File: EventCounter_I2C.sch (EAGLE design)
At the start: 33 parts, among them J1 CONN_42.54_SCREW, J2 CONN_32.54_SCREW, Q1 DMG3404, U10 TXS0102DQM, U11 TPS7A0533DBV, U4 TLV3691DCK, U7 SN74AUP1G34SC70, U8 SN74AUP3G34DCU, U9 ATTINY441/841VQFN

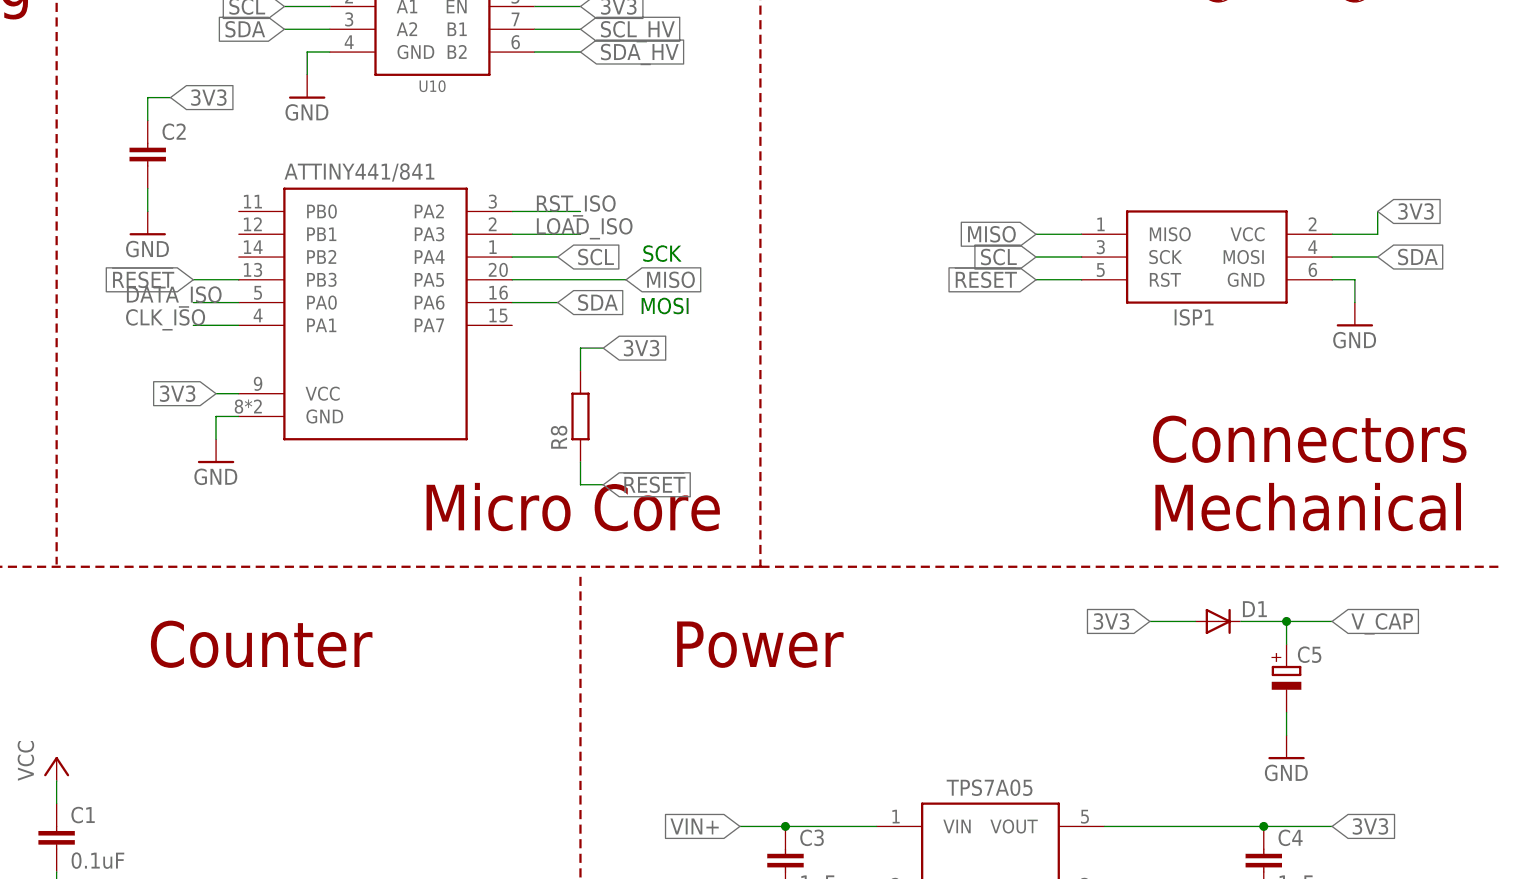
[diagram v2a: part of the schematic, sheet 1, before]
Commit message: Updated values/digikey info
Updated the part
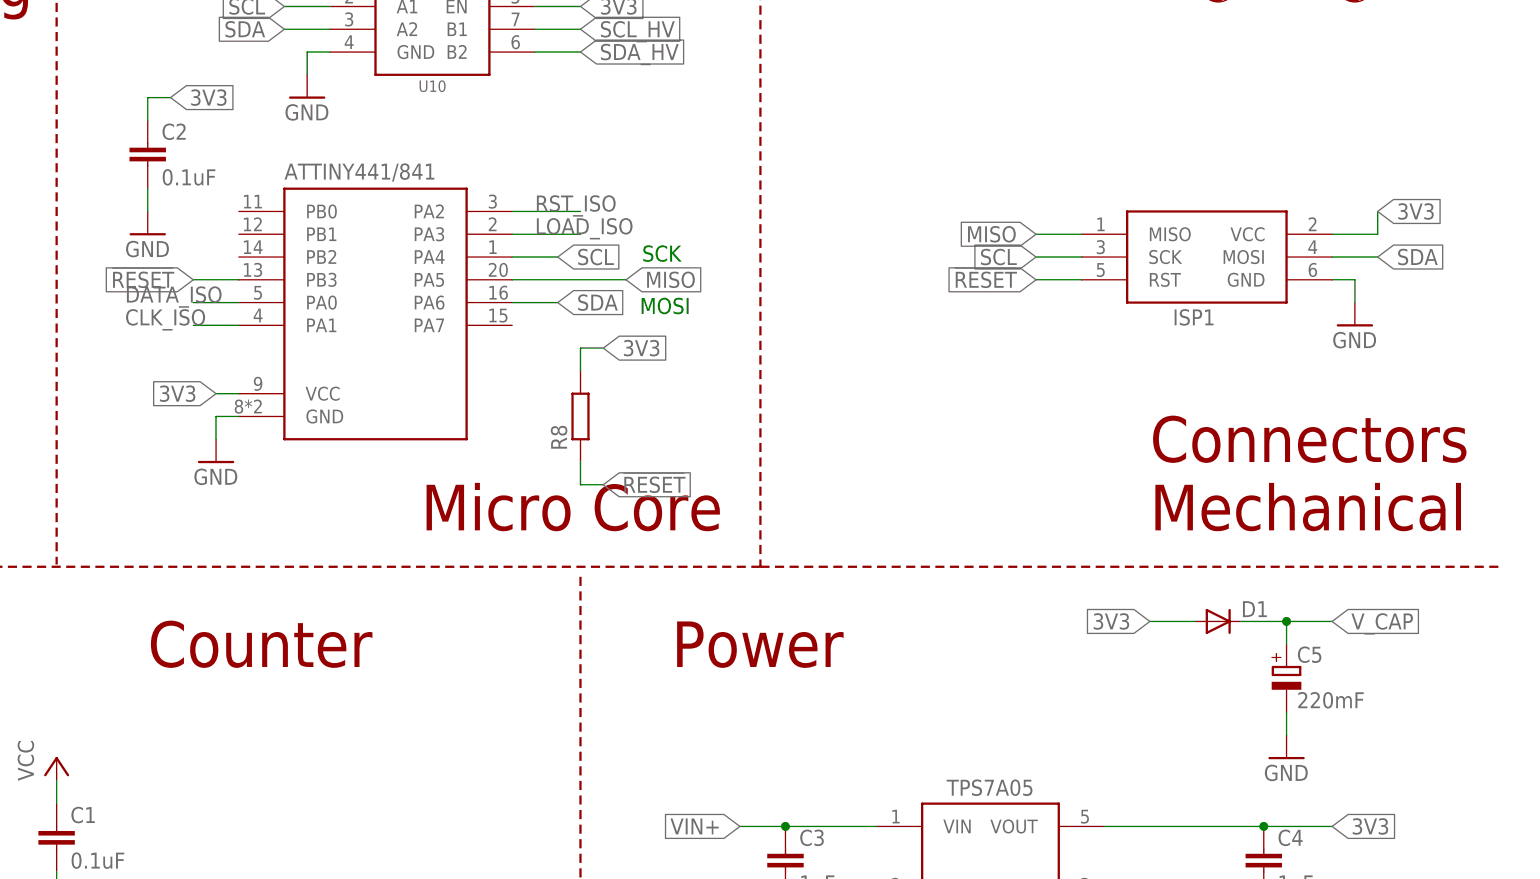
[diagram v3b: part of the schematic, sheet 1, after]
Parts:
- C2: value (none) -> 0.1uF
- C5: value (none) -> 220mF
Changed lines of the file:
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@@
 <grid distance="0.1" unitdist="inch" unit="inch" style="lines" multiple="1" display="no" altdistance="0.01" altunitdist="inch" altunit="inch"/>
 <layers>
-<layer number="1" name="Top" color="4" fill="1" visible="no" active="no"/>
-<layer number="2" name="Route2" color="1" fill="3" visible="no" active="no"/>
-<layer number="3" name="Route3" color="4" fill="3" visible="no" active="no"/>
-<layer number="4" name="Route4" color="1" fill="4" visible="no" active="no"/>
-<layer number="5" name="Route5" color="4" fill="4" visible="no" active="no"/>
-<layer number="6" name="Route6" color="1" fill="8" visible="no" active="no"/>
-<layer number="7" name="Route7" color="4" fill="8" visible="no" active="no"/>
-<layer number="8" name="Route8" color="1" fill="2" visible="no" active="no"/>
-<layer number="9" name="Route9" color="4" fill="2" visible="no" active="no"/>
-<layer number="10" name="Route10" color="1" fill="7" visible="no" active="no"/>
-<layer number="11" name="Route11" color="4" fill="7" visible="no" active="no"/>
-<layer number="12" name="Route12" color="1" fill="5" visible="no" active="no"/>
-<layer number="13" name="Route13" color="4" fill="5" visible="no" active="no"/>
-<layer number="14" name="Route14" color="1" fill="6" visible="no" active="no"/>
-<layer number="15" name="Route15" color="4" fill="6" visible="no" active="no"/>
-<layer number="16" name="Bottom" color="1" fill="1" visible="no" active="no"/>
-<layer number="17" name="Pads" color="2" fill="1" visible="no" active="no"/>
-<layer number="18" name="Vias" color="2" fill="1" visible="no" active="no"/>
-<layer number="19" name="Unrouted" color="6" fill="1" visible="no" active="no"/>
-<layer number="20" name="Dimension" color="24" fill="1" visible="no" active="no"/>
-<layer number="21" name="tPlace" color="7" fill="1" visible="no" active="no"/>
-<layer number="22" name="bPlace" color="7" fill="1" visible="no" active="no"/>
-<layer number="23" name="tOrigins" color="15" fill="1" visible="no" active="no"/>
-<layer number="24" name="bOrigins" color="15" fill="1" visible="no" active="no"/>
-<layer number="25" name="tNames" color="7" fill="1" visible="no" active="no"/>
-<layer number="26" name="bNames" color="7" fill="1" visible="no" active="no"/>
-<layer number="27" name="tValues" color="7" fill="1" visible="no" active="no"/>
-<layer number="28" name="bValues" color="7" fill="1" visible="no" active="no"/>
+<layer number="1" name="Top" color="4" fill="1" visible="yes" active="no"/>
+<layer number="2" name="Route2" color="1" fill="3" visible="yes" active="no"/>
+<layer number="3" name="Route3" color="4" fill="3" visible="yes" active="no"/>
+<layer number="4" name="Route4" color="1" fill="4" visible="yes" active="no"/>
+<layer number="5" name="Route5" color="4" fill="4" visible="yes" active="no"/>
+<layer number="6" name="Route6" color="1" fill="8" visible="yes" active="no"/>
+<layer number="7" name="Route7" color="4" fill="8" visible="yes" active="no"/>
+<layer number="8" name="Route8" color="1" fill="2" visible="yes" active="no"/>
+<layer number="9" name="Route9" color="4" fill="2" visible="yes" active="no"/>
+<layer number="10" name="Route10" color="1" fill="7" visible="yes" active="no"/>
+<layer number="11" name="Route11" color="4" fill="7" visible="yes" active="no"/>
+<layer number="12" name="Route12" color="1" fill="5" visible="yes" active="no"/>
+<layer number="13" name="Route13" color="4" fill="5" visible="yes" active="no"/>
+<layer number="14" name="Route14" color="1" fill="6" visible="yes" active="no"/>
+<layer number="15" name="Route15" color="4" fill="6" visible="yes" active="no"/>
+<layer number="16" name="Bottom" color="1" fill="1" visible="yes" active="no"/>
+<layer number="17" name="Pads" color="2" fill="1" visible="yes" active="no"/>
+<layer number="18" name="Vias" color="2" fill="1" visible="yes" active="no"/>
+<layer number="19" name="Unrouted" color="6" fill="1" visible="yes" active="no"/>
+<layer number="20" name="Dimension" color="24" fill="1" visible="yes" active="no"/>
+<layer number="21" name="tPlace" color="7" fill="1" visible="yes" active="no"/>
+<layer number="22" name="bPlace" color="7" fill="1" visible="yes" active="no"/>
+<layer number="23" name="tOrigins" color="15" fill="1" visible="yes" active="no"/>
+<layer number="24" name="bOrigins" color="15" fill="1" visible="yes" active="no"/>
+<layer number="25" name="tNames" color="7" fill="1" visible="yes" active="no"/>
+<layer number="26" name="bNames" color="7" fill="1" visible="yes" active="no"/>
+<layer number="27" name="tValues" color="7" fill="1" visible="yes" active="no"/>
+<layer number="28" name="bValues" color="7" fill="1" visible="yes" active="no"/>
 <layer number="29" name="tStop" color="7" fill="3" visible="no" active="no"/>
 <layer number="30" name="bStop" color="7" fill="6" visible="no" active="no"/>
@@
 <layer number="35" name="tGlue" color="7" fill="4" visible="no" active="no"/>
 <layer number="36" name="bGlue" color="7" fill="5" visible="no" active="no"/>
-<layer number="37" name="tTest" color="7" fill="1" visible="no" active="no"/>
-<layer number="38" name="bTest" color="7" fill="1" visible="no" active="no"/>
+<layer number="37" name="tTest" color="7" fill="1" visible="yes" active="no"/>
+<layer number="38" name="bTest" color="7" fill="1" visible="yes" active="no"/>
 <layer number="39" name="tKeepout" color="4" fill="11" visible="no" active="no"/>
 <layer number="40" name="bKeepout" color="1" fill="11" visible="no" active="no"/>
@@
 <layer number="44" name="Drills" color="7" fill="1" visible="no" active="no"/>
 <layer number="45" name="Holes" color="7" fill="1" visible="no" active="no"/>
-<layer number="46" name="Milling" color="3" fill="1" visible="no" active="no"/>
-<layer number="47" name="Measures" color="7" fill="1" visible="no" active="no"/>
-<layer number="48" name="Document" color="7" fill="1" visible="no" active="no"/>
-<layer number="49" name="Reference" color="7" fill="1" visible="no" active="no"/>
-<layer number="50" name="dxf" color="7" fill="1" visible="no" active="no"/>
-<layer number="51" name="tDocu" color="7" fill="1" visible="no" active="no"/>
-<layer number="52" name="bDocu" color="7" fill="1" visible="no" active="no"/>
-<layer number="53" name="tGND_GNDA" color="7" fill="1" visible="no" active="no"/>
-<layer number="54" name="bGND_GNDA" color="7" fill="1" visible="no" active="no"/>
-<layer number="56" name="wert" color="7" fill="1" visible="no" active="no"/>
-<layer number="57" name="tCAD" color="7" fill="1" visible="no" active="no"/>
-<layer number="59" name="tCarbon" color="7" fill="1" visible="no" active="no"/>
-<layer number="60" name="bCarbon" color="7" fill="1" visible="no" active="no"/>
+<layer number="46" name="Milling" color="3" fill="1" visible="yes" active="no"/>
+<layer number="47" name="Measures" color="7" fill="1" visible="yes" active="no"/>
+<layer number="48" name="Document" color="7" fill="1" visible="yes" active="no"/>
+<layer number="49" name="Reference" color="7" fill="1" visible="yes" active="no"/>
+<layer number="50" name="dxf" color="7" fill="1" visible="yes" active="no"/>
+<layer number="51" name="tDocu" color="7" fill="1" visible="yes" active="no"/>
+<layer number="52" name="bDocu" color="7" fill="1" visible="yes" active="no"/>
+<layer number="53" name="tGND_GNDA" color="7" fill="1" visible="yes" active="no"/>
+<layer number="54" name="bGND_GNDA" color="7" fill="1" visible="yes" active="no"/>
+<layer number="56" name="wert" color="7" fill="1" visible="yes" active="no"/>
+<layer number="57" name="tCAD" color="7" fill="1" visible="yes" active="no"/>
+<layer number="59" name="tCarbon" color="7" fill="1" visible="yes" active="no"/>
+<layer number="60" name="bCarbon" color="7" fill="1" visible="yes" active="no"/>
 <layer number="88" name="SimResults" color="9" fill="1" visible="yes" active="yes"/>
 <layer number="89" name="SimProbes" color="9" fill="1" visible="yes" active="yes"/>
@@
 <part name="GND20" library="supply1" library_urn="urn:adsk.eagle:library:371" deviceset="GND" device=""/>
 <part name="D1" library="bschulz" deviceset="DIODE" device="SOD-123"/>
-<part name="C5" library="bschulz_passives" deviceset="CPOL-EU" device="HL"/>
+<part name="C5" library="bschulz_passives" deviceset="CPOL-EU" device="HL" value="220mF"/>
 <part name="GND24" library="supply1" library_urn="urn:adsk.eagle:library:371" deviceset="GND" device=""/>
 <part name="U9" library="bschulz" deviceset="ATTINY441/841" device="VQFN"/>
@@
 <part name="J2" library="bschulz" deviceset="CONN_3" device="2.54_SCREW"/>
 <part name="GND22" library="supply1" library_urn="urn:adsk.eagle:library:371" deviceset="GND" device=""/>
-<part name="C2" library="bschulz_passives" deviceset="C-EU" device="C0402" technology="0.1UF"/>
+<part name="C2" library="bschulz_passives" deviceset="C-EU" device="C0402" technology="0.1UF" value="0.1uF"/>
 <part name="GND14" library="supply1" library_urn="urn:adsk.eagle:library:371" deviceset="GND" device=""/>
 <part name="U1" library="bschulz" deviceset="SN74*2G14" device="SC70" technology="AUP"/>

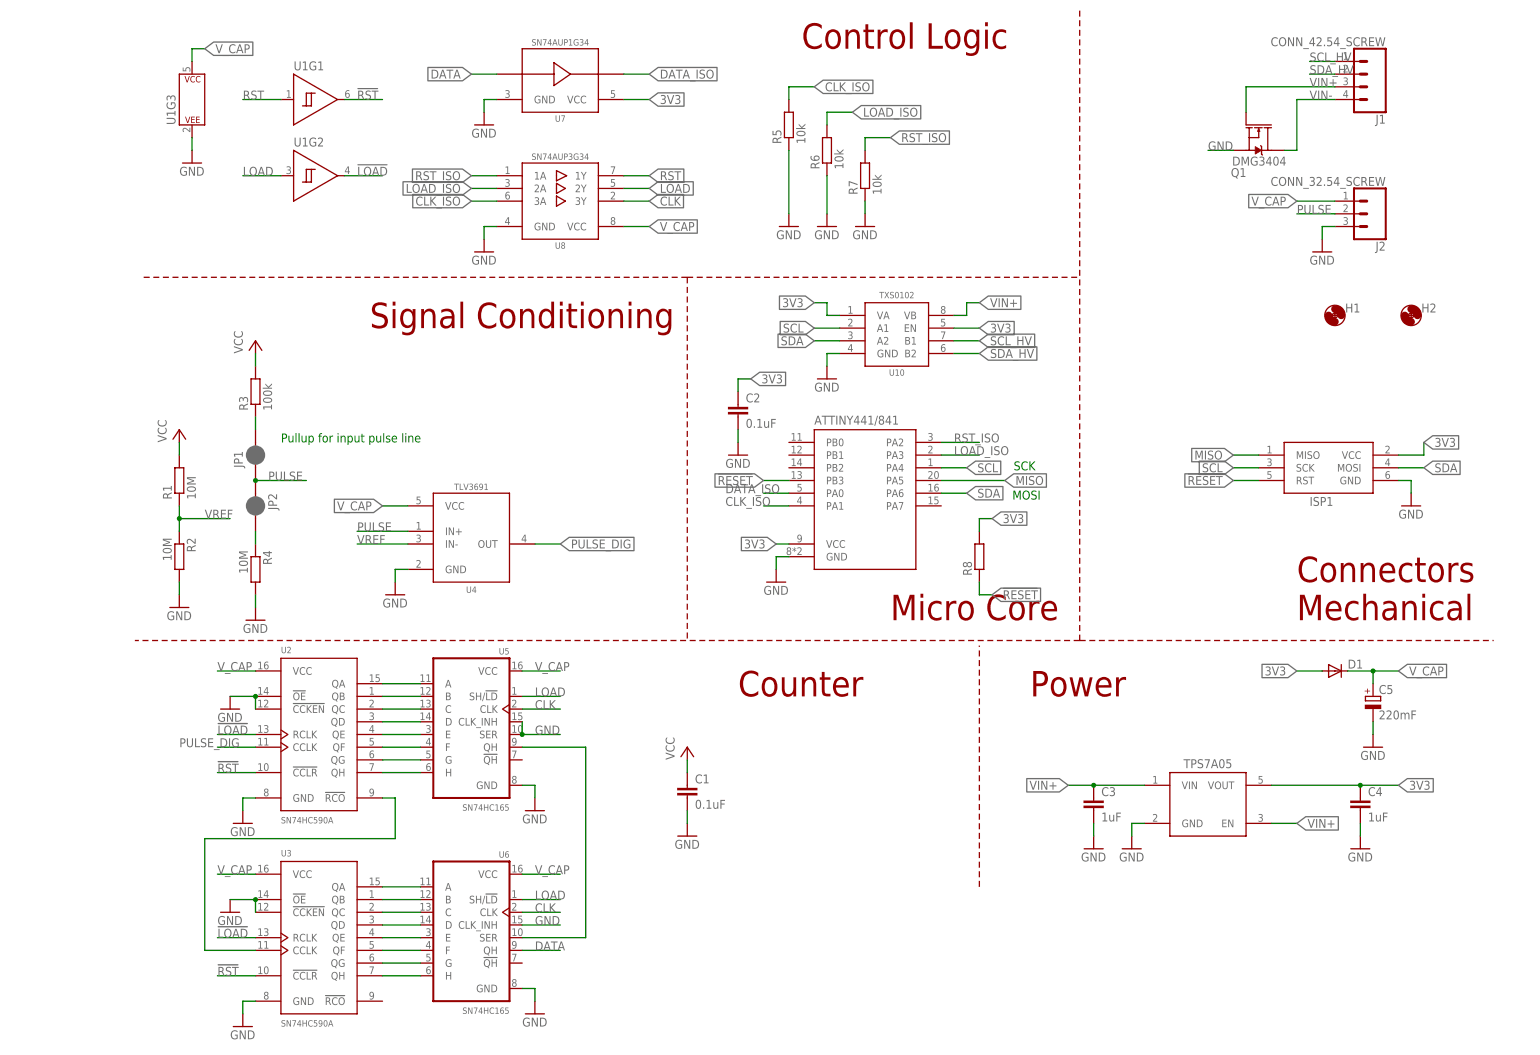
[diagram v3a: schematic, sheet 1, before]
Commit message: Updated firmware, minor design update
Improved firmware capabilities, added minor design updates to schematic, routing and feature decision still required
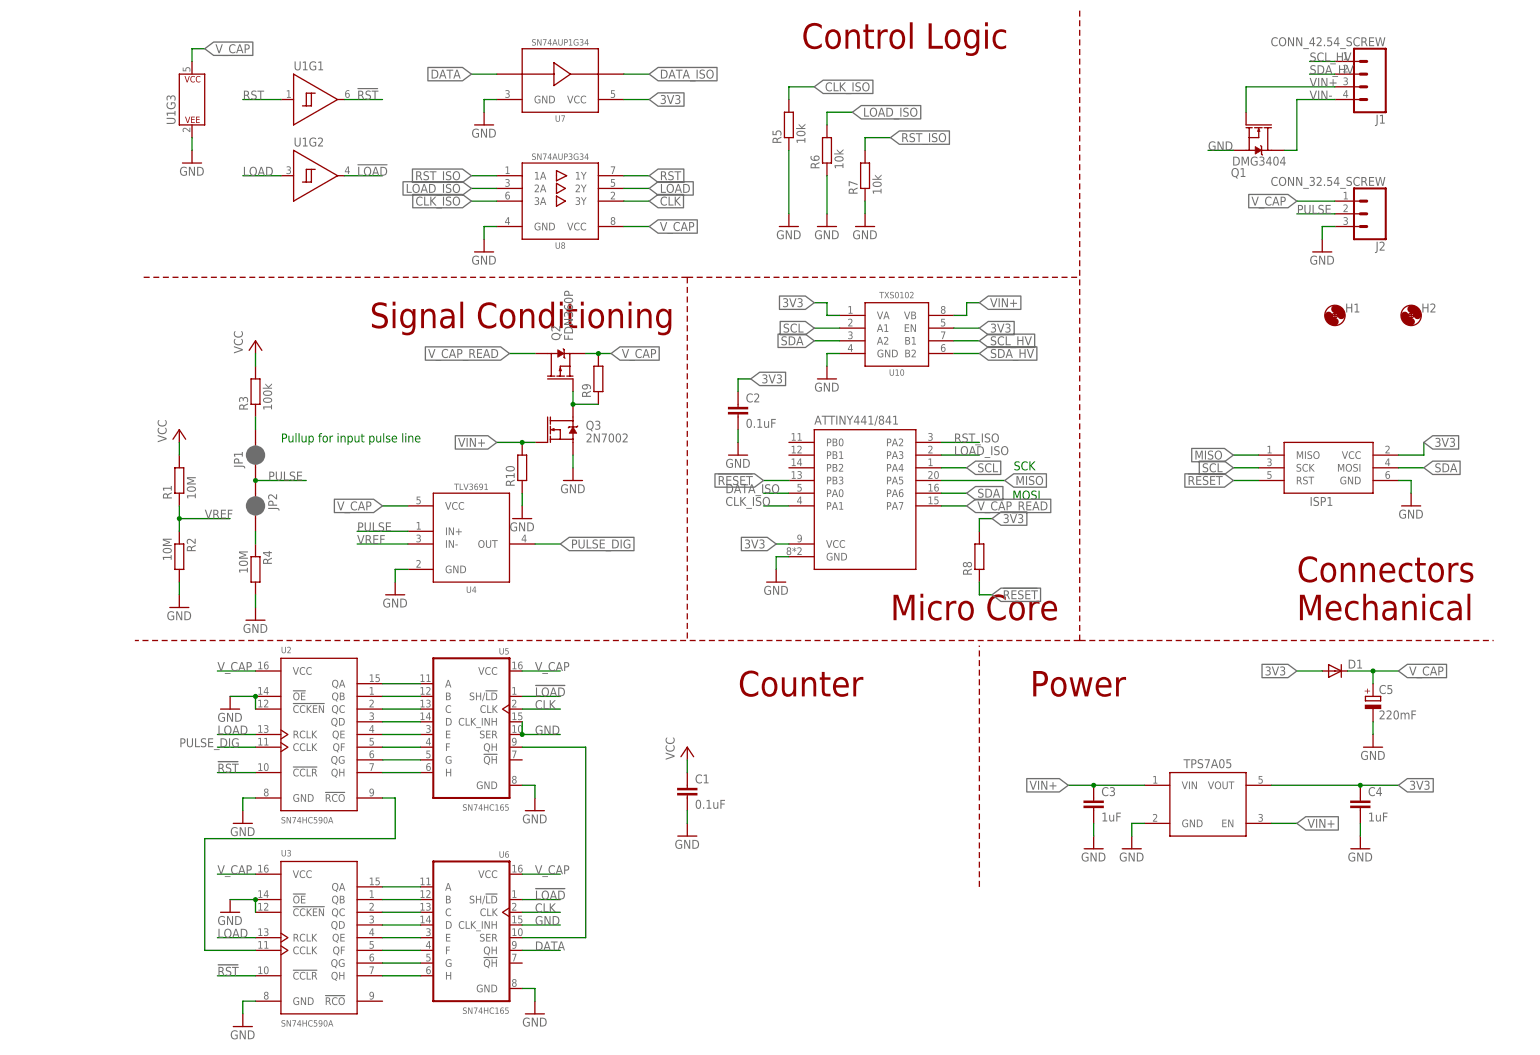
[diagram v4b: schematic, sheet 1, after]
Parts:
- added Q2: FDN360P, bschulz:MOSFET_PCH-FDN360P
- added Q3: 2N7002, bschulz:MOSFET-NCH-2N7002PW
- added R10, R9: (no value), bschulz_passives:R-EU_R0402
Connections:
- new net N$21: Q2.G, Q3.D, R9.1
- new net V_CAP_READ: Q2.D, U9.PA7
- net !LOAD: now also U5.SH/!LD, U6.SH/!LD; no longer U2.RCLK, U3.RCLK
- net GND: now also Q3.S, R10.1
- net LOAD: now also U2.RCLK, U3.RCLK; no longer U5.SH/!LD, U6.SH/!LD
- net VIN+: now also Q3.G, R10.2
- net V_CAP: now also Q2.S, R9.2
